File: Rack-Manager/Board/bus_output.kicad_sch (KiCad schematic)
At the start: 1 part, among them U10 DMG6601

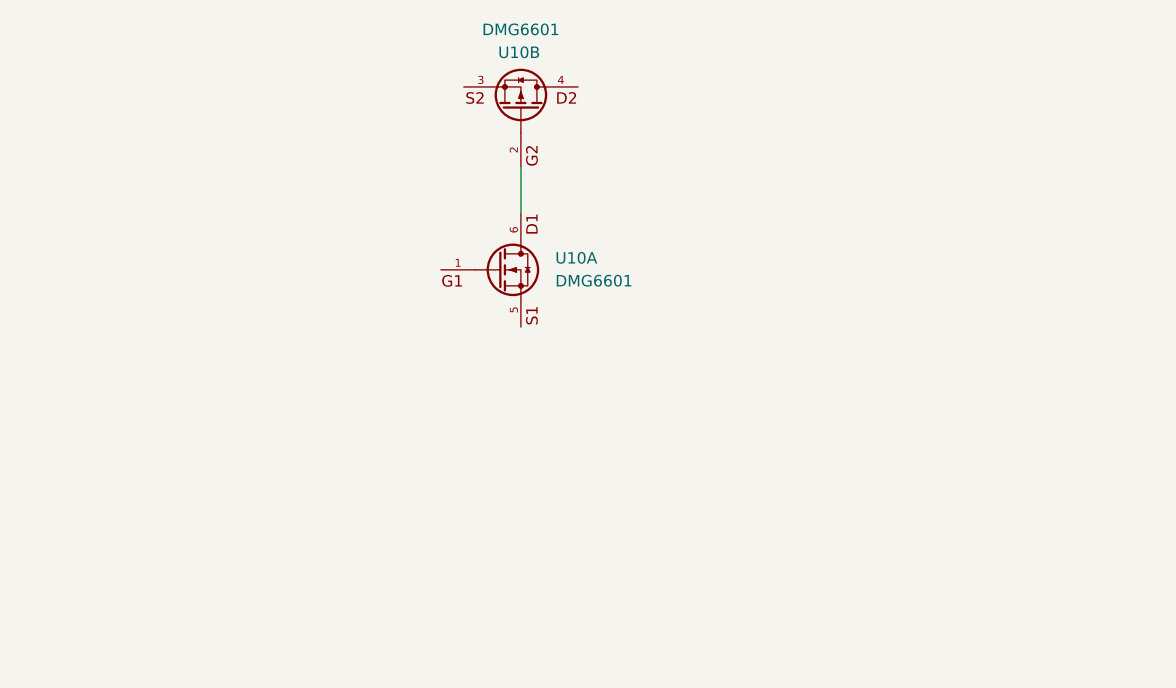
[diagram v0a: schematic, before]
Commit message: Completed fan control circuit
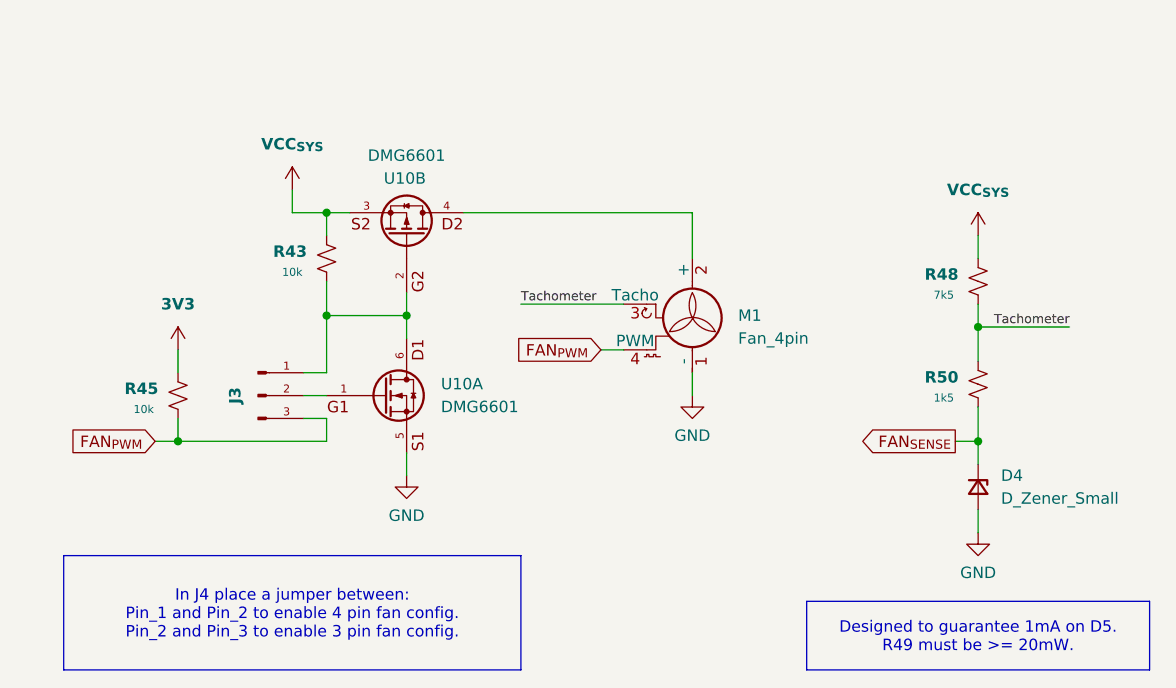
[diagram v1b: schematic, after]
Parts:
- added D4: D_Zener_Small, Diode_SMD:D_SOD-123, symbol Device:D_Zener_Small
- added J3: Conn_01x03_Pin, Connector_PinSocket_2.54mm:PinSocket_1x03_P2.54mm_Vertical, symbol Connector:Conn_01x03_Pin
- added M1: Fan_4pin, Connector:FanPinHeader_1x04_P2.54mm_Vertical, symbol Motor:Fan_4pin
- added R43, R45: 10k, Resistor_SMD:R_0402_1005Metric, symbol Device:R_Small_US
- added R48: 7k5, Resistor_SMD:R_0402_1005Metric, symbol Device:R_Small_US
- added R50: 1k5, Resistor_SMD:R_0402_1005Metric, symbol Device:R_Small_US
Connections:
- net at U10.1: now also J3.2 (Pin_2)
- net GND: now reaches U10.5
- net GND: now also D4.2 (A), M1.1 (-)
- net at U10.2, U10.6: now also J3.1 (Pin_1), R43.1
- net VCC_{SYS}: now reaches U10.3
- net VCC_{SYS}: now also R43.2, R48.2
- net at U10.4: now also M1.2 (+)
- new net 3V3: R45.2
- new net FAN_{PWM}: J3.3 (Pin_3), M1.4 (PWM), R45.1
- new net FAN_{SENSE}: D4.1 (K), R50.1
- new net Tachometer: M1.3 (Tacho), R48.1, R50.2
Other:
- moved on the sheet: U10A, U10B
